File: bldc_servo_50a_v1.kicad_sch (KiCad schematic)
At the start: 93 parts, among them IC1 DRV8305NQPHPRQ1, J1 CAN_JST-1, J2 CAN_JST-2, J3 Encoder_JST_1, J4 Encoder_JST_2, J5 Fan_JST, J6 SWD, Q1 BSC010N04LS, Q2 BSC010N04LS, Q3 BSC010N04LS, Q4 BSC010N04LS, Q5 BSC010N04LS, Q6 BSC010N04LS, SW1 SW_SPDT, U1 LM3480-3.3_Yet to decide, U2 SN65HVD230, U3 STM32G431CBT6

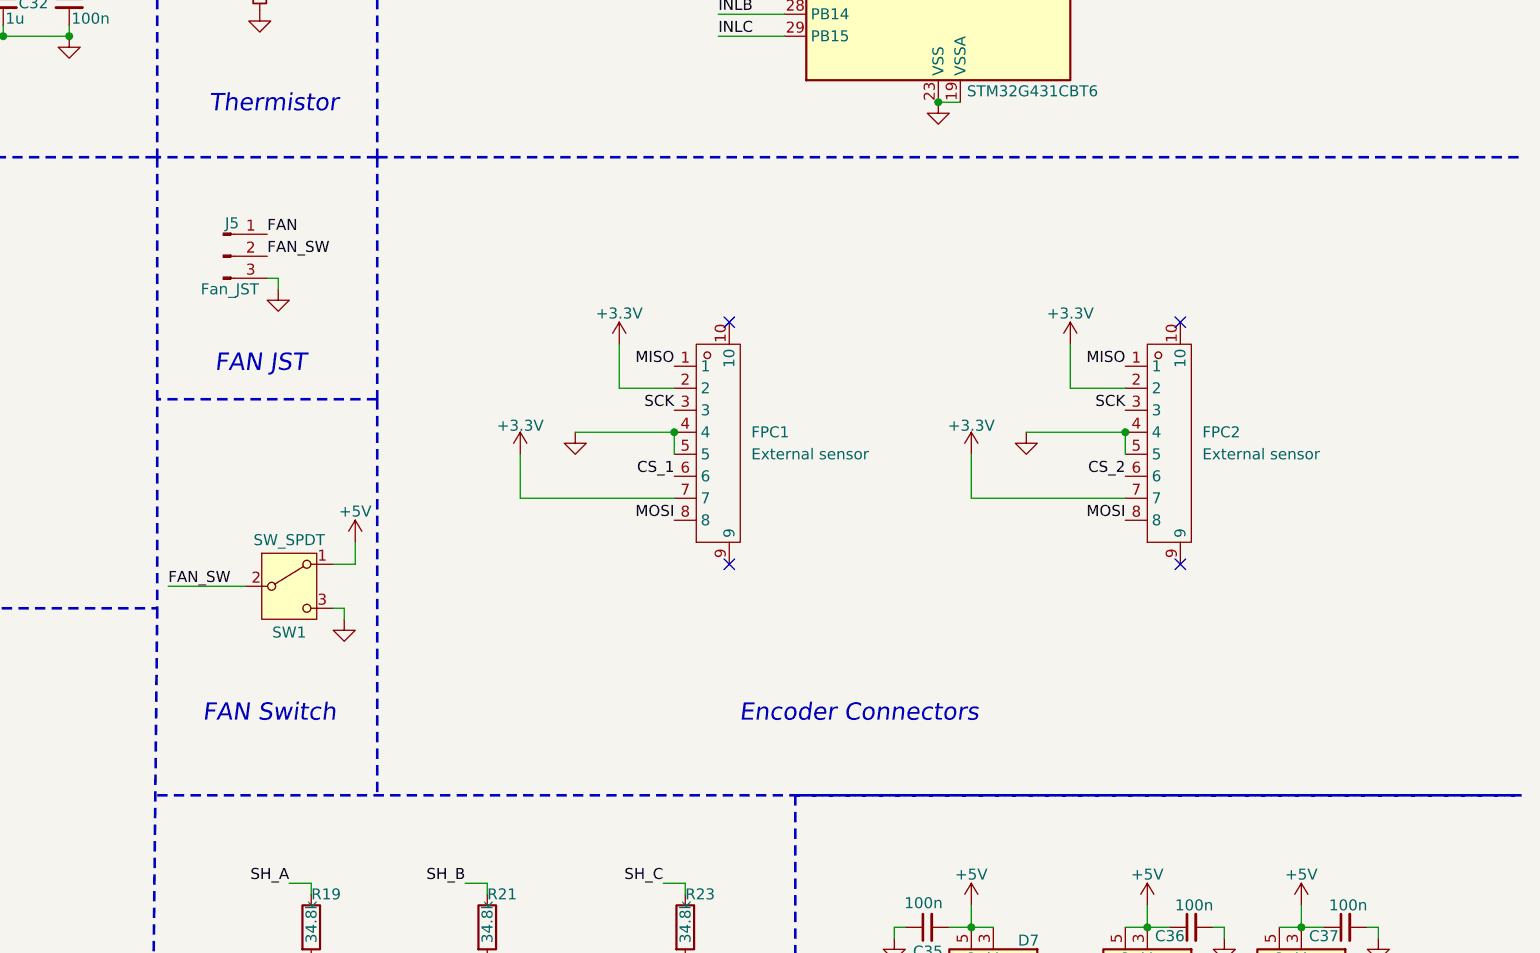
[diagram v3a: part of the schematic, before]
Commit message: Some corrections with FAN Switch
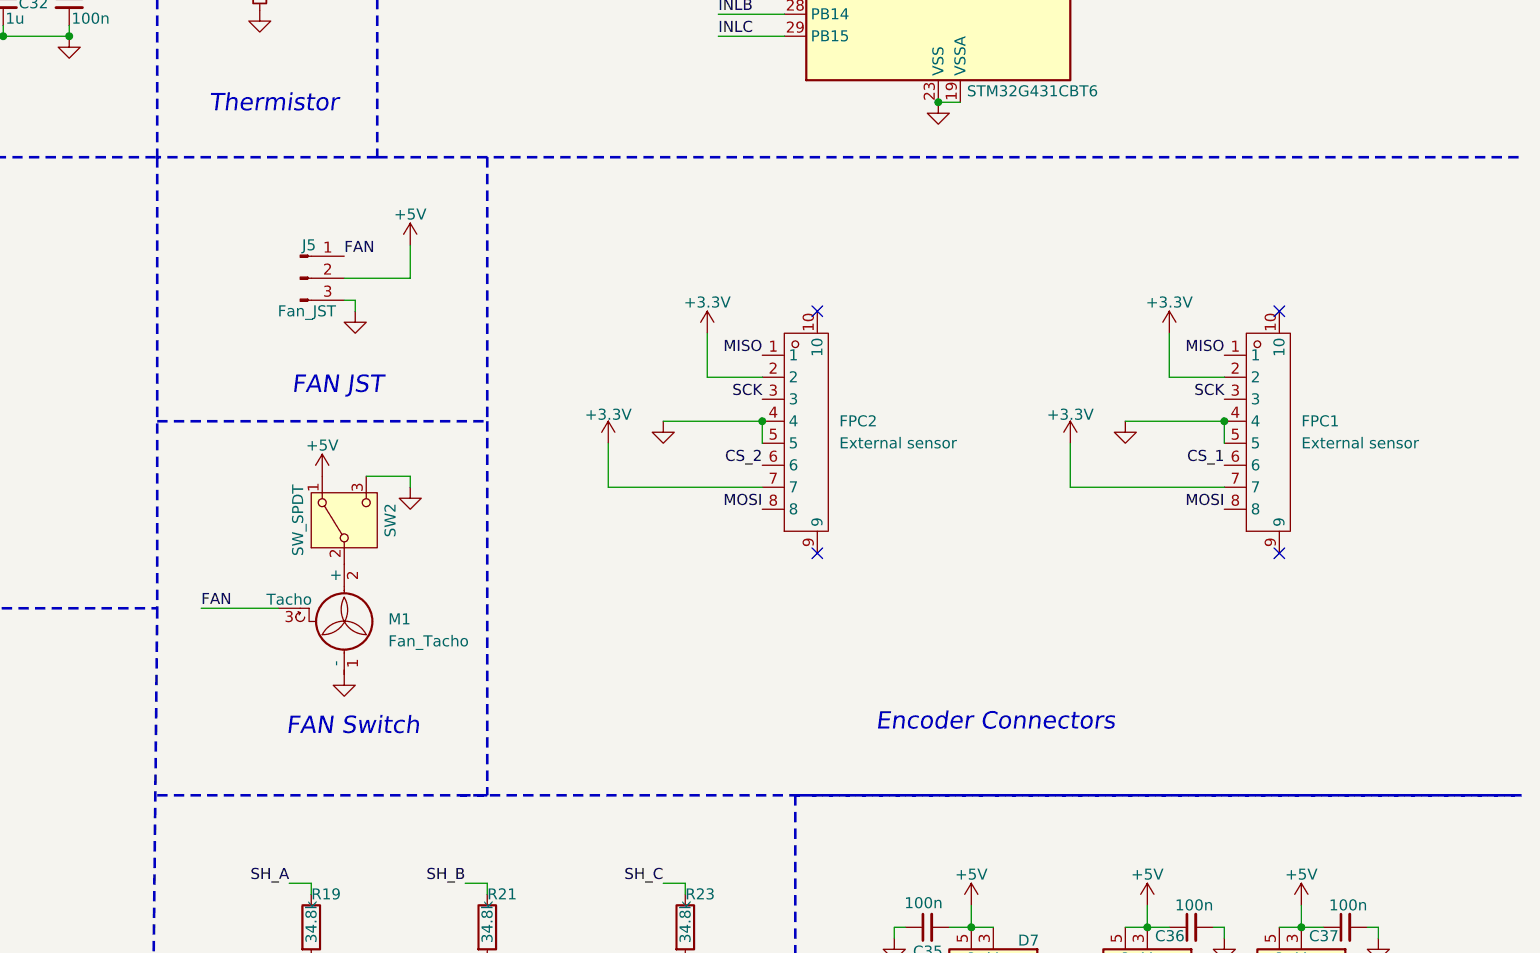
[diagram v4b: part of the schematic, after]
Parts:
- removed SW1: SW_SPDT, symbol Switch:SW_SPDT
- added M1: Fan_Tacho, symbol Motor:Fan_Tacho
- added SW2: SW_SPDT, symbol Switch:SW_SPDT
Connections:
- net FAN_SW is gone; now on net +5V: J5.2 (Pin_2)
- net +5V: now also SW2.1 (A)
- net FAN: now also M1.3 (Tacho)
- net GND: now also M1.1 (-), SW2.3 (C)
- new net: M1.2 (+), SW2.2 (B)
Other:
- moved on the sheet: FPC1, FPC2, J5

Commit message: Added some footprints
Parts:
- C16, C17, C29, C31, C5, C6, C7, C8, C9: footprint (none) -> Capacitor_SMD:C_0402_1005Metric_Pad0.74x0.62mm_HandSolder
- R1, R10, R11, R12, R16, R18, R2, R3, R5, R6, R7, R8, R9: footprint (none) -> Resistor_SMD:R_0402_1005Metric_Pad0.72x0.64mm_HandSolder
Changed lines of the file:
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@@
 			)
 		)
-		(property "Footprint" ""
+		(property "Footprint" "Resistor_SMD:R_0402_1005Metric_Pad0.72x0.64mm_HandSolder"
 			(at 37.592 109.22 90)
 			(effects
@@
 			)
 		)
-		(property "Footprint" ""
+		(property "Footprint" "Resistor_SMD:R_0402_1005Metric_Pad0.72x0.64mm_HandSolder"
 			(at 140.462 135.89 90)
 			(effects
@@
 			)
 		)
-		(property "Footprint" ""
+		(property "Footprint" "Resistor_SMD:R_0402_1005Metric_Pad0.72x0.64mm_HandSolder"
 			(at 24.892 81.28 90)
 			(effects
@@
 			)
 		)
-		(property "Footprint" ""
+		(property "Footprint" "Capacitor_SMD:C_0402_1005Metric_Pad0.74x0.62mm_HandSolder"
 			(at 63.5 44.45 0)
 			(effects
@@
 			)
 		)
-		(property "Footprint" ""
+		(property "Footprint" "Capacitor_SMD:C_0402_1005Metric_Pad0.74x0.62mm_HandSolder"
 			(at 147.32 223.52 0)
 			(effects
@@
 			)
 		)
-		(property "Footprint" ""
+		(property "Footprint" "Resistor_SMD:R_0402_1005Metric_Pad0.72x0.64mm_HandSolder"
 			(at 190.5 25.908 90)
 			(effects
@@
 			)
 		)
-		(property "Footprint" ""
+		(property "Footprint" "Resistor_SMD:R_0402_1005Metric_Pad0.72x0.64mm_HandSolder"
 			(at 140.462 213.36 90)
 			(effects
@@
 			)
 		)
-		(property "Footprint" ""
+		(property "Footprint" "Resistor_SMD:R_0402_1005Metric_Pad0.72x0.64mm_HandSolder"
 			(at 211.582 247.65 90)
 			(effects
@@
 			)
 		)
-		(property "Footprint" ""
+		(property "Footprint" "Capacitor_SMD:C_0402_1005Metric_Pad0.74x0.62mm_HandSolder"
 			(at 76.2 35.56 0)
 			(effects
@@
 			)
 		)
-		(property "Footprint" ""
+		(property "Footprint" "Resistor_SMD:R_0402_1005Metric_Pad0.72x0.64mm_HandSolder"
 			(at 140.462 125.73 90)
 			(effects
@@
 			)
 		)
-		(property "Footprint" ""
+		(property "Footprint" "Resistor_SMD:R_0402_1005Metric_Pad0.72x0.64mm_HandSolder"
 			(at 140.462 223.52 90)
 			(effects
@@
 			)
 		)
-		(property "Footprint" ""
+		(property "Footprint" "Resistor_SMD:R_0402_1005Metric_Pad0.72x0.64mm_HandSolder"
 			(at 64.262 223.52 90)
 			(effects
@@
 			)
 		)
-		(property "Footprint" ""
+		(property "Footprint" "Resistor_SMD:R_0402_1005Metric_Pad0.72x0.64mm_HandSolder"
 			(at 127.762 247.65 90)
 			(effects
@@
 			)
 		)
-		(property "Footprint" ""
+		(property "Footprint" "Resistor_SMD:R_0402_1005Metric_Pad0.72x0.64mm_HandSolder"
 			(at 224.282 223.52 90)
 			(effects
@@
 			)
 		)
-		(property "Footprint" ""
+		(property "Footprint" "Capacitor_SMD:C_0402_1005Metric_Pad0.74x0.62mm_HandSolder"
 			(at 73.66 29.21 0)
 			(effects
@@
 			)
 		)
-		(property "Footprint" ""
+		(property "Footprint" "Capacitor_SMD:C_0402_1005Metric_Pad0.74x0.62mm_HandSolder"
 			(at 222.25 173.99 0)
 			(effects
@@
 			)
 		)
-		(property "Footprint" ""
+		(property "Footprint" "Capacitor_SMD:C_0402_1005Metric_Pad0.74x0.62mm_HandSolder"
 			(at 71.12 44.45 0)
 			(effects
@@
 			)
 		)
-		(property "Footprint" ""
+		(property "Footprint" "Capacitor_SMD:C_0402_1005Metric_Pad0.74x0.62mm_HandSolder"
 			(at 71.12 223.52 0)
 			(effects
@@
 			)
 		)
-		(property "Footprint" ""
+		(property "Footprint" "Capacitor_SMD:C_0402_1005Metric_Pad0.74x0.62mm_HandSolder"
 			(at 231.14 223.52 0)
 			(effects
@@
 			)
 		)
-		(property "Footprint" ""
+		(property "Footprint" "Capacitor_SMD:C_0402_1005Metric_Pad0.74x0.62mm_HandSolder"
 			(at 138.43 173.99 0)
 			(effects
@@
 			)
 		)
-		(property "Footprint" ""
+		(property "Footprint" "Resistor_SMD:R_0402_1005Metric_Pad0.72x0.64mm_HandSolder"
 			(at 51.562 247.65 90)
 			(effects
@@
 			)
 		)
-		(property "Footprint" ""
+		(property "Footprint" "Resistor_SMD:R_0402_1005Metric_Pad0.72x0.64mm_HandSolder"
 			(at 64.262 213.36 90)
 			(effects

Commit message: added more footprints
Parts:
- Q1: footprint Mosfet_PWR:BSC010N04LS -> Package_SON:Infineon_PG-TDSON-8_6.15x5.15mm
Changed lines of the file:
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@@
 			)
 		)
-		(property "Footprint" "Mosfet_PWR:BSC010N04LS"
+		(property "Footprint" "Package_SON:Infineon_PG-TDSON-8_6.15x5.15mm"
 			(at 49.53 279.07 0)
 			(effects

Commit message: added some footprints
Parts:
- removed C36, C37: 100n, symbol Device:C_Small
- removed D8, D9: WS2812, LED_SMD:LED_WS2812_PLCC6_5.0x5.0mm_P1.6mm, symbol LED:WS2812
- removed J3: Encoder_JST_1, Connector_FFC-FPC:TE_0-1734839-8_1x08-1MP_P0.5mm_Horizontal, symbol Connector:Conn_01x08_Pin
- removed J4: Encoder_JST_2, Connector_FFC-FPC:TE_0-1734839-8_1x08-1MP_P0.5mm_Horizontal, symbol Connector:Conn_01x08_Pin
- added R25, R26, R27: 10, Resistor_SMD:R_0603_1608Metric_Pad0.98x0.95mm_HandSolder, symbol Device:R
- C1, C10, C17, C19, C2, C3, C31, C32, C7: LCSC  (none) -> C106254
- C11, C12: footprint (none) -> Capacitor_THT:C_Radial_D10.0mm_H16.0mm_P5.00mm; LCSC  (none) -> C51953324
- C13, C14, C18, C20, C22, C23, C24, C25, C33, C34, C35: footprint (none) -> Capacitor_SMD:C_0402_1005Metric_Pad0.74x0.62mm_HandSolder; LCSC  (none) -> C77020
- C15, C30: footprint (none) -> Capacitor_SMD:C_0402_1005Metric_Pad0.74x0.62mm_HandSolder; LCSC  (none) -> C77019
- C16, C29, C4: footprint Capacitor_SMD:C_0402_1005Metric_Pad0.74x0.62mm_HandSolder -> Capacitor_SMD:C_0603_1608Metric_Pad1.08x0.95mm_HandSolder; LCSC  (none) -> C559769
- C21: footprint (none) -> Capacitor_SMD:C_0805_2012Metric_Pad1.18x1.45mm_HandSolder; LCSC  (none) -> C84416
- C26, C27, C28: footprint (none) -> Capacitor_SMD:C_0402_1005Metric_Pad0.74x0.62mm_HandSolder; LCSC  (none) -> C77023
- C5, C6: LCSC  (none) -> C106260
- C8: LCSC  (none) -> C132170
- GH1: renamed from ThermistorwhatRtokeep1; value R_Small -> 10k; footprint (none) -> Resistor_SMD:R_0402_1005Metric_Pad0.72x0.64mm_HandSolder; LCSC  (none) -> C60490
- Q2, Q3, Q4, Q5, Q6: footprint Mosfet_PWR:BSC010N04LS -> Package_SON:Infineon_PG-TDSON-8_6.15x5.15mm
- R1, R2: LCSC  (none) -> C60490
- R16, R3, R7: LCSC  (none) -> C4146794
- R28: renamed from 10k1; value R_Small -> 10k1; LCSC  (none) -> C60490
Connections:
- net GH_A: now also R25.1; no longer Q1.4 (G)
- net GH_B: now also R26.1; no longer Q3.4 (G)
- net GH_C: now also R27.1; no longer Q5.4 (G)
- new net: Q1.4 (G), R25.2
- new net: Q3.4 (G), R26.2
- new net: Q5.4 (G), R27.2
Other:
- note added: "Addressable LEDs"
- note added: "Power sw"
- note added: "add 5v regulator"
- note added: "power distribution switch"
- note removed: "Addressabkle LEDs"
- note removed: "JST to Encoder"
- moved on the sheet: C35, D7

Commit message: added more footprints, 5v buck.
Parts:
- added C26: 680u, symbol Device:C_Small
- added C35: 220u, Capacitor_SMD:C_0402_1005Metric_Pad0.74x0.62mm_HandSolder, symbol Device:C_Small
- added D7: 1N5822, Diode_THT:D_DO-201AD_P15.24mm_Horizontal, symbol Diode:1N5822
- added J3: Conn_01x02_Pin, symbol Connector:Conn_01x02_Pin
- added L1: 33uH, symbol Device:L_Small
- added U3: LM2596S-5, Package_TO_SOT_SMD:TO-263-5_TabPin3, symbol Regulator_Switching:LM2596S-5
- renumbered C26 to C27, C27 to C28, C28 to C29, C29 to C30, C30 to C31, C31 to C32, C32 to C33, C33 to C34, C34 to C36, C35 to C37, D7 to D8, FPC2 to FPC1, FPC1 to FPC2, J5 to J4, J6 to J5, R25 to R1, R8 to R10, R9 to R11, R10 to R12, R11 to R13, R27 to R14, R12 to R15, R13 to R16, R14 to R17, R15 to R18, R16 to R19, R1 to R2, R17 to R20, R18 to R21, R19 to R22, R20 to R23, R28 to R24, R21 to R25, R22 to R26, R23 to R27, R24 to R28, R2 to R3, R3 to R4, R4 to R5, R5 to R6, R6 to R7, R26 to R8, R7 to R9, SW2 to SW1, U3 to U4
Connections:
- net +24V: now also C26.1, J3.1 (Pin_1), U3.1 (VIN)
- net +5V: now also C35.2, L1.2, U3.4 (FB)
- net GND: now also C26.2, C35.1, D7.2 (A), J3.2 (Pin_2), U3.3 (GND), U3.5 (~{ON}/OFF)
- new net: D7.1 (K), L1.1, U3.2 (OUT)
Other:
- note added: "5v regulator"
- note added: "Addressable LED"
- note added: "add 5v regulator-done"
- note removed: "Addressable LEDs"
- note removed: "add 5v regulator"
- moved on the sheet: C36, GH1, J5, R24
